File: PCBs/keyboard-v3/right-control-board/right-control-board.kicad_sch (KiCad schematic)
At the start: 3 parts

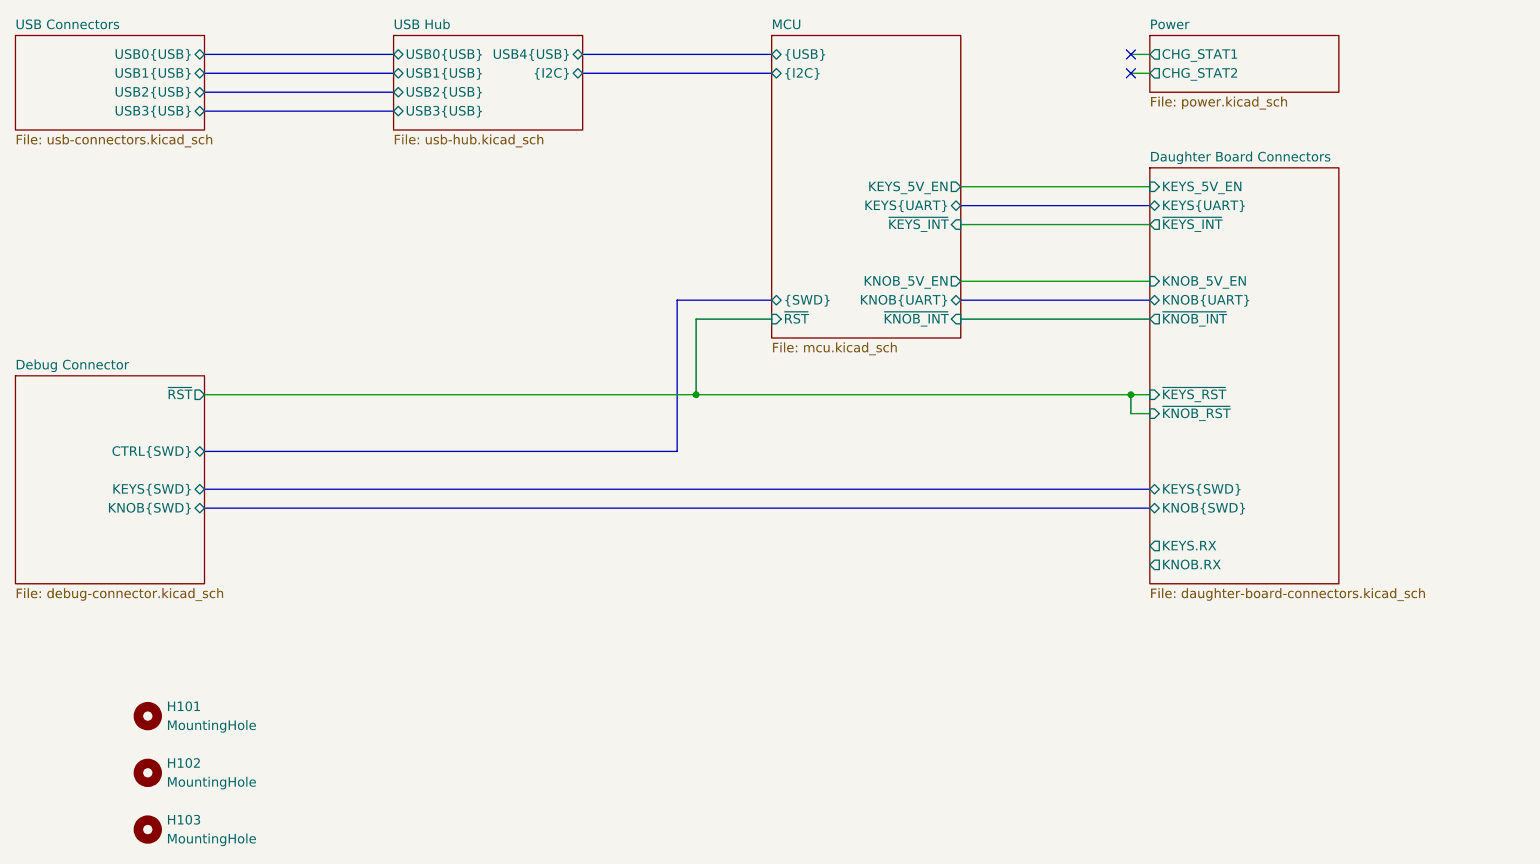
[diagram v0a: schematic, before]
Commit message: Right control board placement and schematic done
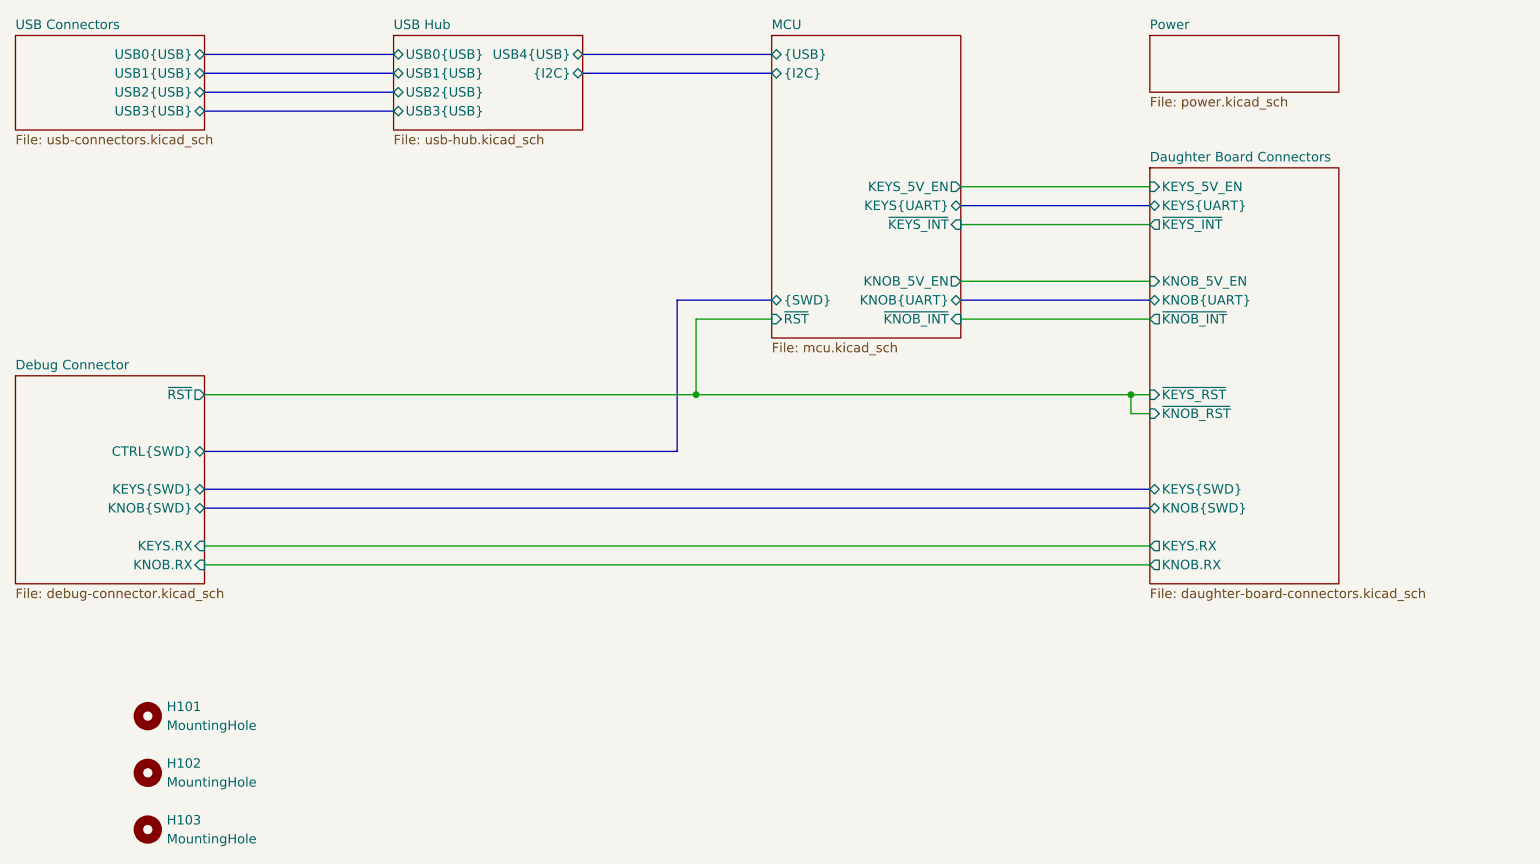
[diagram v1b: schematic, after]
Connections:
- no-connect marks 2 -> 0
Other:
- sheet Debug Connector ports: added KEYS.RX, KNOB.RX; removed none
- sheet Power ports: added none; removed CHG_STAT1, CHG_STAT2
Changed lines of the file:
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@@
 		(color 0 0 0 0)
 	)
-	(no_connect
-		(at 213.36 60.96)
-	)
-	(no_connect
-		(at 213.36 63.5)
-	)
 	(bus
 		(pts
@@
 		)
 	)
-	(wire
-		(pts
-			(xy 213.36 63.5) (xy 215.9 63.5)
-		)
-		(stroke
-			(width 0)
-			(type default)
-		)
-	)
 	(bus
 		(pts
@@
 	(wire
 		(pts
+			(xy 88.9 127) (xy 215.9 127)
+		)
+		(stroke
+			(width 0)
+			(type default)
+		)
+	)
+	(wire
+		(pts
 			(xy 154.94 106.68) (xy 213.36 106.68)
 		)
@@
 	(wire
 		(pts
+			(xy 88.9 129.54) (xy 215.9 129.54)
+		)
+		(stroke
+			(width 0)
+			(type default)
+		)
+	)
+	(wire
+		(pts
 			(xy 213.36 109.22) (xy 213.36 106.68)
 		)
@@
 		(pts
 			(xy 190.5 78.74) (xy 215.9 78.74)
-		)
-		(stroke
-			(width 0)
-			(type default)
-		)
-	)
-	(wire
-		(pts
-			(xy 213.36 60.96) (xy 215.9 60.96)
 		)
 		(stroke
@@
 			)
 		)
-		(pin "CHG_STAT1" output
-			(at 215.9 60.96 180)
-			(effects
-				(font
-					(size 1.27 1.27)
-				)
-				(justify left)
-			)
-		)
-		(pin "CHG_STAT2" output
-			(at 215.9 63.5 180)
-			(effects
-				(font
-					(size 1.27 1.27)
-				)
-				(justify left)
-			)
-		)
 		(instances
 			(project "right-control-board"
@@
 			(effects
 				(font
+					(size 1.27 1.27)
+				)
+				(justify right)
+			)
+		)
+		(pin "KEYS.RX" input
+			(at 88.9 127 0)
+			(effects
+				(font
+					(size 1.27 1.27)
+				)
+				(justify right)
+			)
+		)
+		(pin "KNOB.RX" input
+			(at 88.9 129.54 0)
+			(effects
+				(font

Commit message: Right control board ~50 unrouted
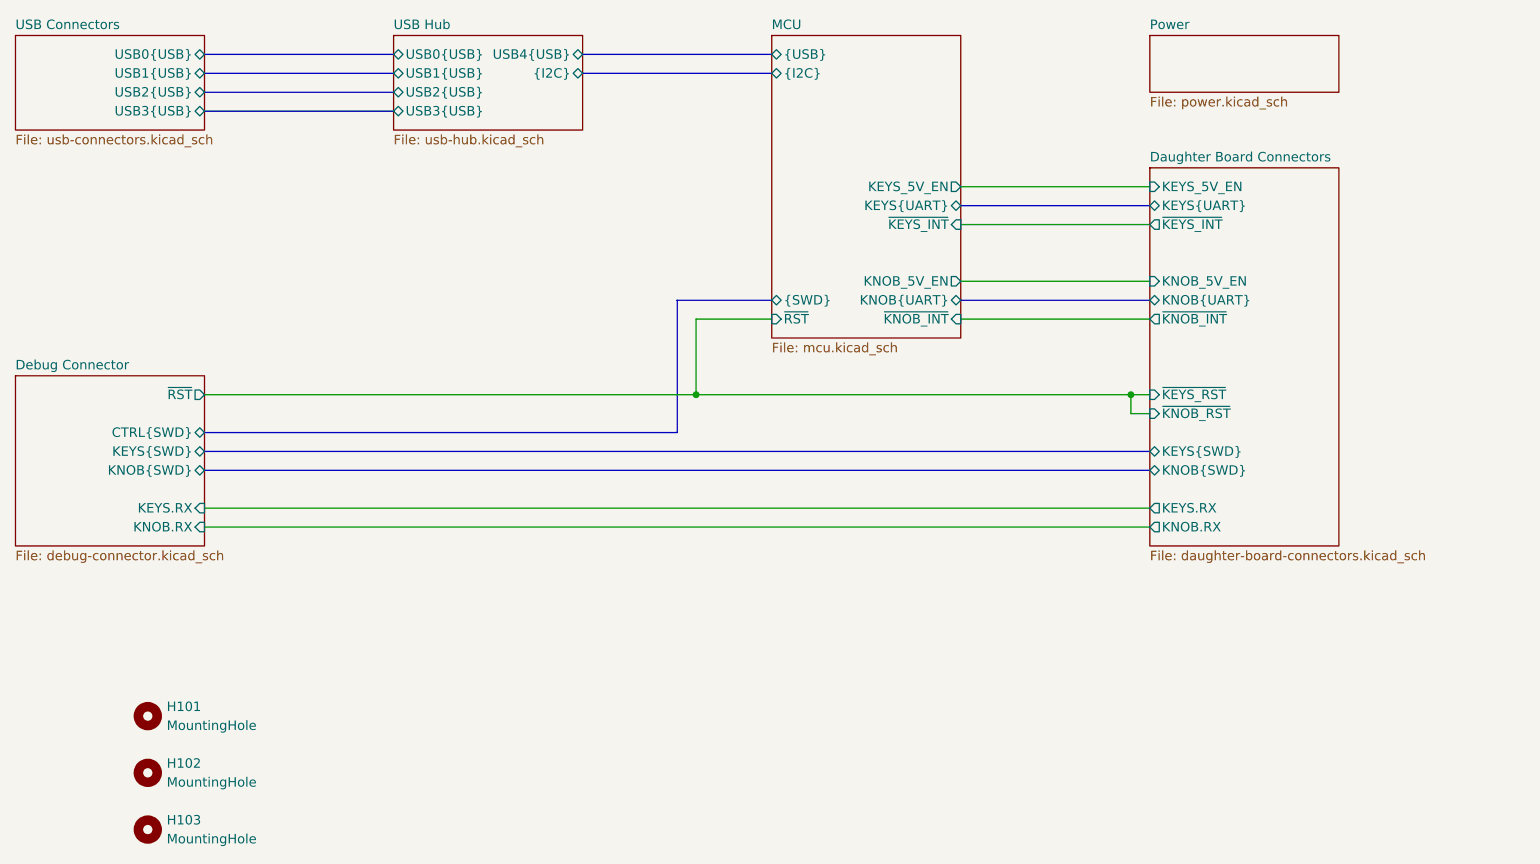
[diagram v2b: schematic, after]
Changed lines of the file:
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@@
 	(bus
+		(pts
+			(xy 88.9 116.84) (xy 215.9 116.84)
+		)
+		(stroke
+			(width 0)
+			(type default)
+		)
+	)
+	(wire
+		(pts
+			(xy 154.94 106.68) (xy 154.94 96.52)
+		)
+		(stroke
+			(width 0)
+			(type default)
+		)
+	)
+	(wire
+		(pts
+			(xy 190.5 96.52) (xy 215.9 96.52)
+		)
+		(stroke
+			(width 0)
+			(type default)
+		)
+	)
+	(bus
+		(pts
+			(xy 88.9 60.96) (xy 114.3 60.96)
+		)
+		(stroke
+			(width 0)
+			(type default)
+		)
+	)
+	(bus
+		(pts
+			(xy 190.5 93.98) (xy 215.9 93.98)
+		)
+		(stroke
+			(width 0)
+			(type default)
+		)
+	)
+	(wire
 		(pts
 			(xy 88.9 121.92) (xy 215.9 121.92)
@@
 	(wire
 		(pts
-			(xy 154.94 106.68) (xy 154.94 96.52)
-		)
-		(stroke
-			(width 0)
-			(type default)
-		)
-	)
-	(wire
-		(pts
-			(xy 190.5 96.52) (xy 215.9 96.52)
-		)
-		(stroke
-			(width 0)
-			(type default)
-		)
-	)
-	(bus
-		(pts
-			(xy 88.9 60.96) (xy 114.3 60.96)
-		)
-		(stroke
-			(width 0)
-			(type default)
-		)
-	)
-	(bus
-		(pts
-			(xy 190.5 93.98) (xy 215.9 93.98)
-		)
-		(stroke
-			(width 0)
-			(type default)
-		)
-	)
-	(wire
-		(pts
-			(xy 88.9 127) (xy 215.9 127)
-		)
-		(stroke
-			(width 0)
-			(type default)
-		)
-	)
-	(wire
-		(pts
 			(xy 154.94 106.68) (xy 213.36 106.68)
 		)
@@
 	(wire
 		(pts
-			(xy 88.9 129.54) (xy 215.9 129.54)
+			(xy 88.9 124.46) (xy 215.9 124.46)
 		)
 		(stroke
@@
 	(bus
 		(pts
-			(xy 88.9 119.38) (xy 215.9 119.38)
+			(xy 88.9 114.3) (xy 215.9 114.3)
 		)
 		(stroke
@@
 	(bus
 		(pts
-			(xy 152.4 114.3) (xy 152.4 93.98)
+			(xy 152.4 111.76) (xy 152.4 93.98)
 		)
 		(stroke
@@
 	(bus
 		(pts
-			(xy 88.9 114.3) (xy 152.4 114.3)
+			(xy 88.9 111.76) (xy 152.4 111.76)
 		)
 		(stroke
@@
 	(sheet
 		(at 215.9 76.2)
-		(size 25.4 55.88)
+		(size 25.4 50.8)
 		(exclude_from_sim no)
 		(in_bom yes)
@@
 		)
 		(property "Sheetfile" "daughter-board-connectors.kicad_sch"
-			(at 215.9 132.6646 0)
+			(at 215.9 127.5846 0)
 			(effects
 				(font
@@
 		)
 		(pin "KEYS{SWD}" bidirectional
-			(at 215.9 119.38 180)
+			(at 215.9 114.3 180)
 			(effects
 				(font
@@
 		)
 		(pin "KNOB{SWD}" bidirectional
-			(at 215.9 121.92 180)
+			(at 215.9 116.84 180)
 			(effects
 				(font
@@
 		)
 		(pin "KEYS.RX" output
-			(at 215.9 127 180)
+			(at 215.9 121.92 180)
 			(effects
 				(font
@@
 		)
 		(pin "KNOB.RX" output
-			(at 215.9 129.54 180)
+			(at 215.9 124.46 180)
 			(effects
 				(font
@@
 	(sheet
 		(at 63.5 104.14)
-		(size 25.4 27.94)
+		(size 25.4 22.86)
 		(exclude_from_sim no)
 		(in_bom yes)
@@
 		)
 		(property "Sheetfile" "debug-connector.kicad_sch"
-			(at 63.5 132.6646 0)
+			(at 63.5 127.5846 0)
 			(effects
 				(font
@@
 		)
 		(pin "CTRL{SWD}" bidirectional
+			(at 88.9 111.76 0)
+			(effects
+				(font
+					(size 1.27 1.27)
+				)
+				(justify right)
+			)
+		)
+		(pin "KEYS{SWD}" bidirectional
 			(at 88.9 114.3 0)
 			(effects
@@
 			)
 		)
-		(pin "KEYS{SWD}" bidirectional
-			(at 88.9 119.38 0)
-			(effects
-				(font
-					(size 1.27 1.27)
-				)
-				(justify right)
-			)
-		)
 		(pin "KNOB{SWD}" bidirectional
-			(at 88.9 121.92 0)
+			(at 88.9 116.84 0)
 			(effects
 				(font
@@
 		)
 		(pin "KEYS.RX" input
-			(at 88.9 127 0)
+			(at 88.9 121.92 0)
 			(effects
 				(font
@@
 		)
 		(pin "KNOB.RX" input
-			(at 88.9 129.54 0)
-			(effects
-				(font
+			(at 88.9 124.46 0)
+			(effects
+				(font
